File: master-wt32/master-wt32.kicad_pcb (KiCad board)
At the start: 2 copper layers, 52.3 x 72.4 mm, 4 parts, among them J1 Conn_01x06_Male, J2 Conn_01x06_Male, J3 Conn_01x06_Female, J4 Conn_01x06_Female

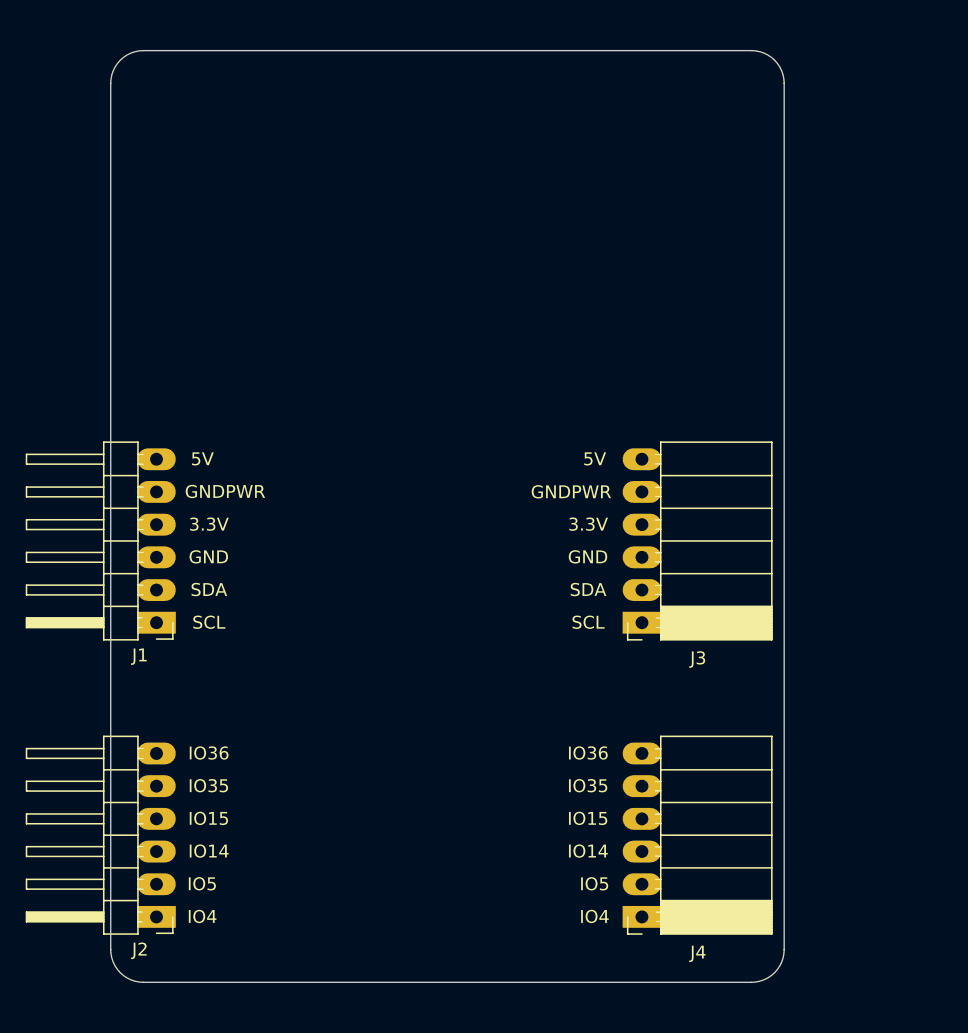
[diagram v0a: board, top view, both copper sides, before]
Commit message: add components to master-wt32
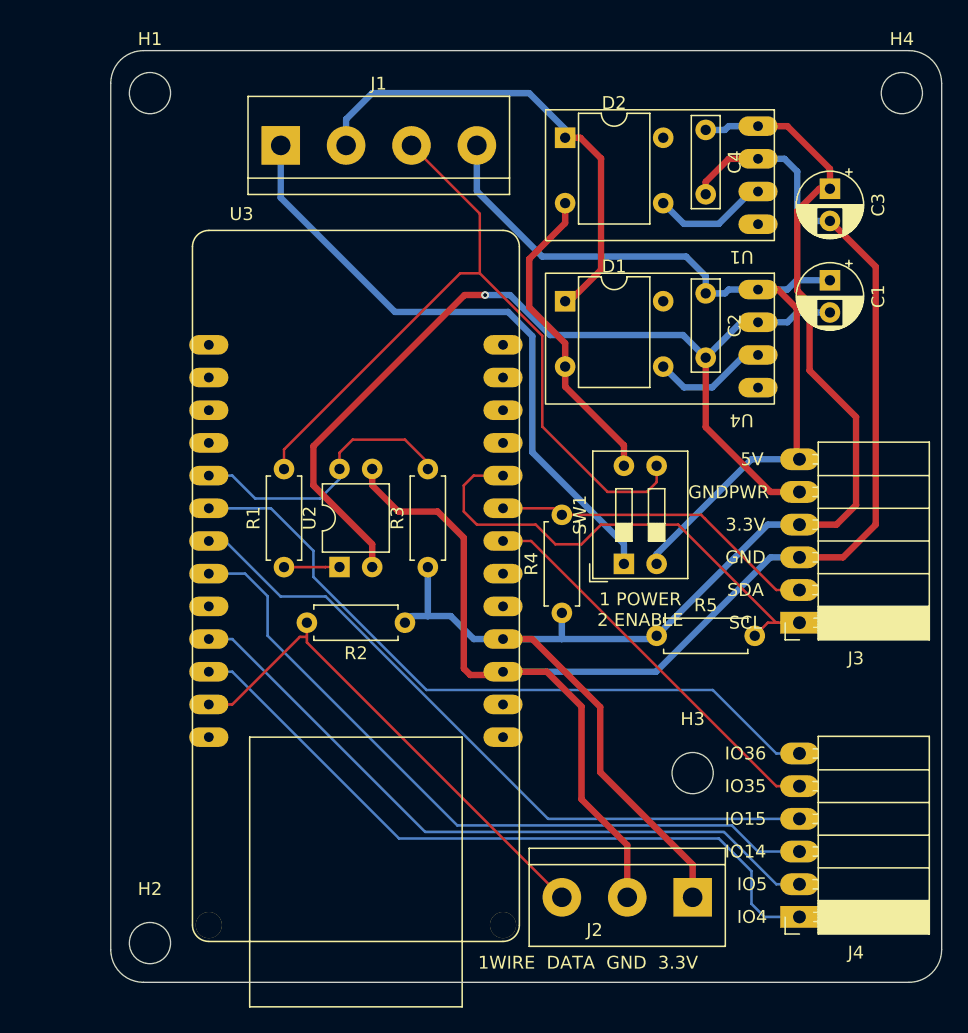
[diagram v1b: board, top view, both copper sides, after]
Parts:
- added C1: 1uF 50V, Capacitor_THT:CP_Radial_D5.0mm_P2.50mm, F.Cu at (119.4, 72.5)
- added C2: 100nF 63V, Capacitor_THT:C_Rect_L7.0mm_W2.0mm_P5.00mm, F.Cu at (109.7, 73.5)
- added C3: 1uF 50V, Capacitor_THT:CP_Radial_D5.0mm_P2.50mm, F.Cu at (119.4, 65.3)
- added C4: 100nF 63V, Capacitor_THT:C_Rect_L7.0mm_W2.0mm_P5.00mm, F.Cu at (109.7, 60.8)
- added D1: DB107, custom:DB107, F.Cu at (98.8, 74.1)
- added D2: DB107, custom:DB107, F.Cu at (98.8, 61.4)
- added H1: MountingHole, MountingHole:MountingHole_3.2mm_M3, F.Cu at (66.5, 57.9)
- added H2: MountingHole, MountingHole:MountingHole_3.2mm_M3, F.Cu at (66.5, 124.0)
- added H3: MountingHole, MountingHole:MountingHole_3.2mm_M3, F.Cu at (108.7, 110.7)
- added H4: MountingHole, MountingHole:MountingHole_3.2mm_M3, F.Cu at (125.0, 57.9)
- added R1: 680, Resistor_THT:R_Axial_DIN0207_L6.3mm_D2.5mm_P7.62mm_Horizontal, F.Cu at (77.0, 94.7)
- added R2: 4k7, Resistor_THT:R_Axial_DIN0207_L6.3mm_D2.5mm_P7.62mm_Horizontal, F.Cu at (86.4, 99.1)
- added R3: 10k, Resistor_THT:R_Axial_DIN0207_L6.3mm_D2.5mm_P7.62mm_Horizontal, F.Cu at (88.1, 94.7)
- added R4: 10k, Resistor_THT:R_Axial_DIN0207_L6.3mm_D2.5mm_P7.62mm_Horizontal, F.Cu at (98.6, 98.3)
- added R5: 10k, Resistor_THT:R_Axial_DIN0207_L6.3mm_D2.5mm_P7.62mm_Horizontal, F.Cu at (105.9, 100.1)
- added SW1: SW_DIP_x02, Button_Switch_THT:SW_DIP_SPSTx02_Slide_9.78x7.26mm_W7.62mm_P2.54mm, F.Cu at (103.4, 94.5)
- added U1: MINI360, boards:MINI360, F.Cu at (106.2, 64.3)
- added U2: PC817, Package_DIP:DIP-4_W7.62mm, F.Cu at (81.3, 94.7)
- added U3: WT32-ETH0-Board, boards:WT32-ETH01-Board-Reversed, F.Cu at (82.5, 96.5)
- added U4: MINI360, boards:MINI360, F.Cu at (106.2, 77.0)
- J1: value Conn_01x06_Male -> Screw_Terminal_01x04; footprint Connector_PinHeader_2.54mm:PinHeader_1x06_P2.54mm_Horizontal -> TerminalBlock:TerminalBlock_bornier-4_P5.08mm
- J2: value Conn_01x06_Male -> Screw_Terminal_01x03; footprint Connector_PinHeader_2.54mm:PinHeader_1x06_P2.54mm_Horizontal -> TerminalBlock:TerminalBlock_bornier-3_P5.08mm
- moved J2 41.7 mm to (108.7, 120.4)
- moved J1 38.3 mm to (76.7, 62.0), turned to 0 degrees
- moved J3 12.2 mm to (117.0, 99.1)
- moved J4 12.2 mm to (117.0, 121.9)
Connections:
- J1 pad 1: SCL -> Net-(J1-Pad1)
- J1 pad 2: SDA -> IN-
- J1 pad 3: GND -> ENABLE_IN
- J1 pad 4: +3V3 -> +5V
- J2 pad 1: GPIO4 -> +3V3
- J2 pad 2: GPIO5 -> GND
- J2 pad 3: GPIO14 -> 1WIRE
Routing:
- net GND: track 0.00 -> 121.0 mm
- net +3V3: track 0.00 -> 114.4 mm
- net GNDPWR: track 0.00 -> 74.5 mm, vias 0 -> 1
- net +5V: track 0.00 -> 65.8 mm
- net ENABLE_IN: track 0.00 -> 61.0 mm
- net GPIO14: track 0.00 -> 56.6 mm
- net GPIO4: track 0.00 -> 55.3 mm
- net GPIO36: track 0.00 -> 55.0 mm
- net GPIO15: track 0.00 -> 54.8 mm
- net GPIO5: track 0.00 -> 53.8 mm
- net Net-(J1-Pad1): track 0.00 -> 48.7 mm
- net 1WIRE: track 0.00 -> 39.3 mm
- net SCL: track 0.00 -> 38.5 mm
- net IN-: track 0.00 -> 37.6 mm
- net GPIO35: track 0.00 -> 30.9 mm
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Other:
- board size 52.3 x 72.4 mm -> 64.6 x 72.4 mm
- board text added: "1 POWER 2 ENABLE"
- board text added: "1WIRE DATA GND 3.3V"

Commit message: route master-wt32
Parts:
- added D3: LED, LED_THT:LED_D5.0mm, F.Cu at (105.9, 87.1)
- added D4: LED, LED_THT:LED_D5.0mm, F.Cu at (98.5, 87.1)
- added R6: 330, Resistor_THT:R_Axial_DIN0207_L6.3mm_D2.5mm_P7.62mm_Horizontal, F.Cu at (110.2, 94.0)
- added R7: 680, Resistor_THT:R_Axial_DIN0207_L6.3mm_D2.5mm_P7.62mm_Horizontal, F.Cu at (98.6, 94.0)
- moved R5 21.8 mm to (84.3, 102.9), turned to 90 degrees
- moved R1 13.5 mm to (76.7, 81.3)
- moved R2 13.5 mm to (86.1, 85.6)
- moved R3 13.5 mm to (87.9, 81.3)
- moved U2 13.5 mm to (81.0, 81.3)
- moved R4 11.4 mm to (88.1, 102.9)
- moved SW1 7.37 mm to (103.1, 101.9)
- moved C1 1.08 mm to (120.1, 73.2)
- moved C3 0.92 mm to (120.1, 65.9)
- moved C2 0.28 mm to (109.7, 73.2)
- moved C4 0.28 mm to (109.7, 60.5)
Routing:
- net +5V: track 65.8 -> 109.4 mm
- net Net-(J1-Pad1): track 48.7 -> 75.1 mm
- net GND: track 121.0 -> 139.7 mm
- net SCL: track 38.5 -> 56.8 mm
- net +3V3: track 114.4 -> 132.2 mm
- net 1WIRE: track 39.3 -> 53.1 mm
- net SDA: track 25.7 -> 36.7 mm
- net ENABLE: track 22.1 -> 31.5 mm
- net Net-(D3-Pad1): track 0.00 -> 8.65 mm
- net GPIO35: track 30.9 -> 39.3 mm
- net IN+: track 24.6 -> 31.9 mm
- net Net-(D4-Pad1): track 0.00 -> 6.86 mm
- net ENABLE_IN: track 61.0 -> 67.9 mm
- net GNDPWR: track 74.5 -> 67.8 mm, vias 1 -> 0
- net GPIO36: track 55.0 -> 60.2 mm
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
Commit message: refactor master-wt32 pcb
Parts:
- moved H2 86.7 mm to (123.9, 58.9)
- moved H4 65.5 mm to (123.9, 123.4)
- moved H3 43.5 mm to (67.1, 123.4)
- moved R6 36.5 mm to (83.6, 69.1), turned to 180 degrees
- moved R7 25.2 mm to (94.5, 69.1), turned to 180 degrees
- moved J4 5.07 mm to (116.5, 116.9)
- moved J3 2.62 mm to (116.5, 96.5)
- moved H1 1.14 mm to (67.1, 58.9)
- moved R4 0.92 mm to (88.9, 102.4)
- moved R5 0.92 mm to (85.1, 102.4)
- moved U4 0.92 mm to (106.9, 76.5)
- moved D2 0.92 mm to (99.6, 60.9)
- moved U1 0.92 mm to (106.9, 63.8)
- moved C2 0.92 mm to (110.5, 72.7)
- moved C3 0.92 mm to (120.9, 65.3)
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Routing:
- net GND: track 139.7 -> 0.00 mm
- net +3V3: track 132.2 -> 0.00 mm
- net +5V: track 109.4 -> 0.00 mm
- net Net-(J1-Pad1): track 75.1 -> 0.00 mm
- net ENABLE_IN: track 67.9 -> 0.00 mm
- net GNDPWR: track 67.8 -> 0.00 mm
- net GPIO36: track 60.2 -> 0.00 mm
- net GPIO15: track 58.1 -> 0.00 mm
- net GPIO14: track 57.7 -> 0.00 mm
- net SCL: track 56.8 -> 0.00 mm
- net GPIO4: track 54.8 -> 0.00 mm
- net GPIO5: track 53.8 -> 0.00 mm
- net 1WIRE: track 53.1 -> 0.00 mm
- net GPIO35: track 39.3 -> 0.00 mm
- net IN-: track 36.9 -> 0.00 mm
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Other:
- board size 64.6 x 72.4 mm -> 64 x 71.6 mm

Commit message: refactor master-wt32
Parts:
- removed C1: 1uF 50V, Capacitor_THT:CP_Radial_D5.0mm_P2.50mm
- removed C2: 100nF 63V, Capacitor_THT:C_Rect_L7.0mm_W2.0mm_P5.00mm
- removed D2: DB107, custom:DB107
- removed D3: LED, LED_THT:LED_D5.0mm
- removed R6: 330, Resistor_THT:R_Axial_DIN0207_L6.3mm_D2.5mm_P7.62mm_Horizontal
- removed SW1: SW_DIP_x02, Button_Switch_THT:SW_DIP_SPSTx02_Slide_9.78x7.26mm_W7.62mm_P2.54mm
- C3: value 1uF 50V -> 100nF 63V; footprint Capacitor_THT:CP_Radial_D5.0mm_P2.50mm -> Capacitor_THT:C_Rect_L7.0mm_W2.0mm_P5.00mm
- C4: value 100nF 63V -> 10uF 50V; footprint Capacitor_THT:C_Rect_L7.0mm_W2.0mm_P5.00mm -> Capacitor_THT:CP_Radial_D5.0mm_P2.50mm
- U1: value MINI360 -> LM2596-Board; footprint boards:MINI360 -> boards:LM2596-Board
- U4: value MINI360 -> LD1117S33TR_SOT223; footprint boards:MINI360 -> Package_TO_SOT_THT:TO-220-3_Vertical
- moved C4 48.8 mm to (101.6, 108.0), turned to 180 degrees
- moved D4 22.7 mm to (120.7, 78.7)
- moved C3 20.7 mm to (104.1, 77.5)
- moved U4 17.7 mm to (124.1, 72.4), turned to 90 degrees
- moved R7 16.3 mm to (108.5, 77.5), turned to 0 degrees
- moved U1 16.3 mm to (108.0, 80.0), turned to -90 degrees
- moved D1 4.86 mm to (104.3, 72.4), turned to 90 degrees
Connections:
- C3 pad 1: +3V3 -> +5V
- C3 pad 2: GND -> GNDPWR
- C4 pad 2: GND -> GNDPWR
- J1 pad 1: Net-(J1-Pad1) -> IN+
- J2 pad 2: GND -> GNDPWR
- J3 pad 3: GND -> GNDPWR
- U1 pad 1: unconnected-(U1-Pad1) -> Net-(D1-Pad3)
- U1 pad 2: Net-(D2-Pad3) -> Net-(D1-Pad4)
- U1 pad 3: GND -> GNDPWR
- U1 pad 4: +3V3 -> +5V
- U2 pad 3: GND -> GNDPWR
- U3 pad 10: +3V3 -> unconnected-(U3-Pad10)
- U3 pad 11: GND -> GNDPWR
- U3 pad 12: unconnected-(U3-Pad12) -> +5V
- U4 pad 1: unconnected-(U4-Pad1) -> GNDPWR
- U4 pad 2: Net-(D1-Pad3) -> +3V3
- U4 pad 3: GNDPWR -> +5V
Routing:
- net +3V3: track 0.00 -> 141.1 mm
- net GNDPWR: track 0.00 -> 120.7 mm
- net +5V: track 0.00 -> 115.0 mm
- net 1WIRE: track 0.00 -> 65.9 mm
- net GPIO36: track 0.00 -> 59.4 mm
- net GPIO15: track 0.00 -> 56.1 mm
- net GPIO14: track 0.00 -> 53.0 mm
- net GPIO5: track 0.00 -> 50.9 mm
- net GPIO4: track 0.00 -> 50.9 mm
- net IN+: track 0.00 -> 45.5 mm
- net SCL: track 0.00 -> 42.5 mm
- net GPIO35: track 0.00 -> 41.1 mm
- net IN-: track 0.00 -> 33.6 mm
- net SDA: track 0.00 -> 32.2 mm
- net ENABLE: track 0.00 -> 28.1 mm
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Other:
- board text removed: "1 POWER 2 ENABLE"

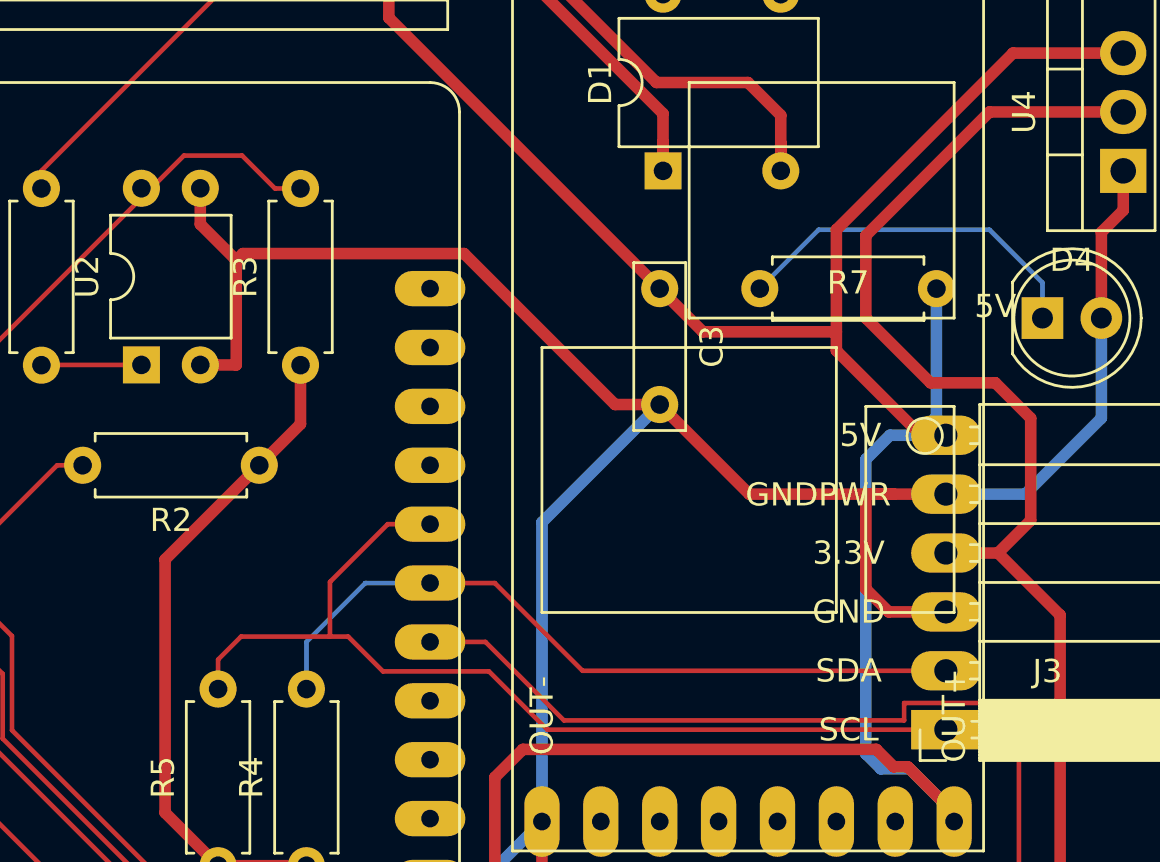
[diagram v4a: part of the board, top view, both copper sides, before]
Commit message: update master-wt32 routing
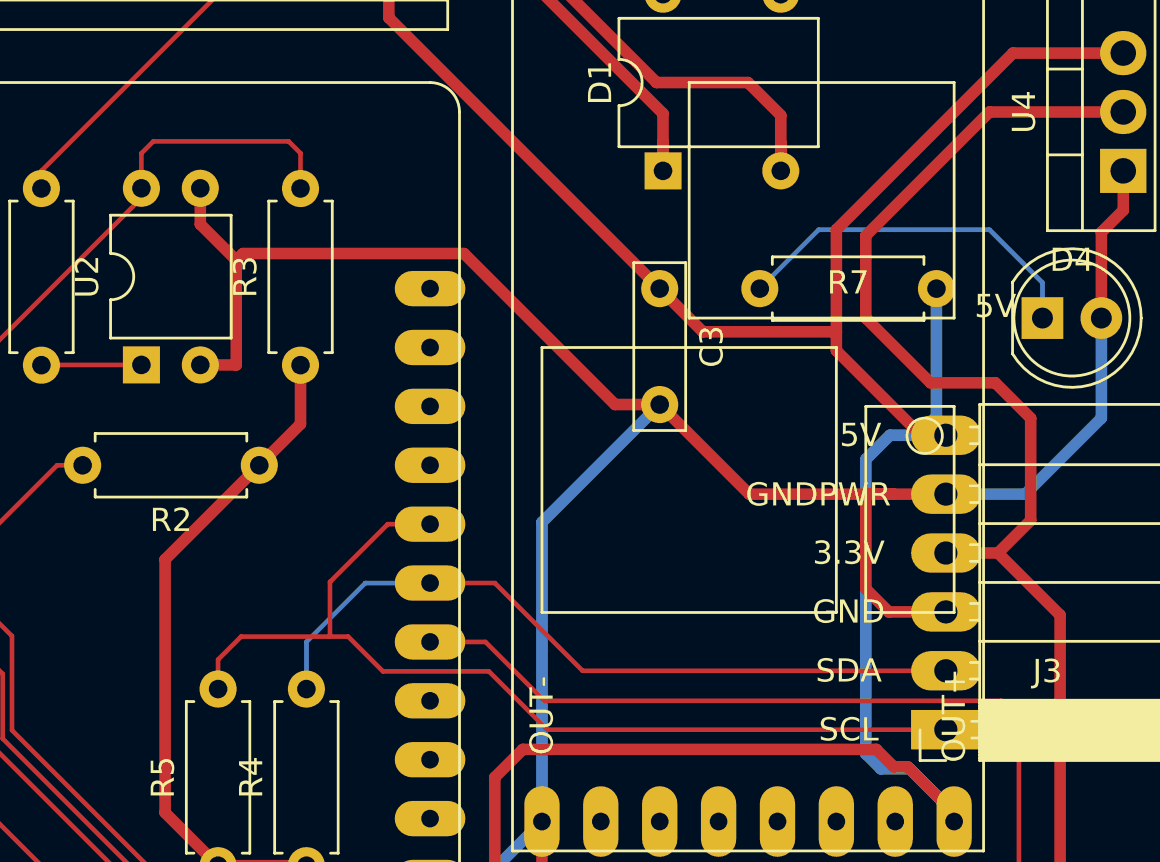
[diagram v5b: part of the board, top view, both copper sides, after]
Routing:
- net ENABLE: track 28.1 -> 30.8 mm
- net GPIO35: track 41.1 -> 40.0 mm
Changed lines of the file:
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@@
-(kicad_pcb (version 20210722) (generator pcbnew)
+(kicad_pcb (version 20210925) (generator pcbnew)
   (general
     (thickness 1.6)
@@
     (fp_circle (center 0 0) (end 3.2 0) (layer "Cmts.User") (width 0.15) (fill none))
     (fp_circle (center 0 0) (end 3.45 0) (layer "F.CrtYd") (width 0.05) (fill none))
-    (pad "1" np_thru_hole circle locked (at 0 0) (size 3.2 3.2) (drill 3.2) (layers *.Cu *.Mask))
+    (pad "" np_thru_hole circle locked (at 0 0) (size 3.2 3.2) (drill 3.2) (layers *.Cu *.Mask))
   )
   (footprint "boards:WT32-ETH01-Board-Reversed" (layer "F.Cu")
@@
     (fp_circle (center 0 0) (end 3.2 0) (layer "Cmts.User") (width 0.15) (fill none))
     (fp_circle (center 0 0) (end 3.45 0) (layer "F.CrtYd") (width 0.05) (fill none))
-    (pad "1" np_thru_hole circle locked (at 0 0) (size 3.2 3.2) (drill 3.2) (layers *.Cu *.Mask))
+    (pad "" np_thru_hole circle locked (at 0 0) (size 3.2 3.2) (drill 3.2) (layers *.Cu *.Mask))
   )
   (footprint "Package_DIP:DIP-4_W7.62mm" (layer "F.Cu")
@@
     (fp_circle (center 0 0) (end 3.2 0) (layer "Cmts.User") (width 0.15) (fill none))
     (fp_circle (center 0 0) (end 3.45 0) (layer "F.CrtYd") (width 0.05) (fill none))
-    (pad "1" np_thru_hole circle locked (at 0 0) (size 3.2 3.2) (drill 3.2) (layers *.Cu *.Mask))
+    (pad "" np_thru_hole circle locked (at 0 0) (size 3.2 3.2) (drill 3.2) (layers *.Cu *.Mask))
   )
   (footprint "LED_THT:LED_D5.0mm" (layer "F.Cu")
@@
     (fp_circle (center 0 0) (end 3.2 0) (layer "Cmts.User") (width 0.15) (fill none))
     (fp_circle (center 0 0) (end 3.45 0) (layer "F.CrtYd") (width 0.05) (fill none))
-    (pad "1" np_thru_hole circle locked (at 0 0) (size 3.2 3.2) (drill 3.2) (layers *.Cu *.Mask))
+    (pad "" np_thru_hole circle locked (at 0 0) (size 3.2 3.2) (drill 3.2) (layers *.Cu *.Mask))
   )
   (footprint "Capacitor_THT:C_Rect_L7.0mm_W2.0mm_P5.00mm" (layer "F.Cu")
@@
   (segment (start 105.918 111.506) (end 91.186 111.506) (width 0.2) (layer "F.Cu") (net 10))
   (segment (start 116.483 104.175) (end 113.249 104.175) (width 0.2) (layer "F.Cu") (net 10))
+  (segment (start 119.634 96.012) (end 118.872 95.25) (width 0.2) (layer "F.Cu") (net 11))
+  (segment (start 119.634 105.664) (end 119.634 96.012) (width 0.2) (layer "F.Cu") (net 11))
+  (segment (start 99.1644 95.25) (end 96.6244 92.71) (width 0.2) (layer "F.Cu") (net 11))
+  (segment (start 96.6244 92.71) (end 94.234 92.71) (width 0.2) (layer "F.Cu") (net 11))
+  (segment (start 118.872 95.25) (end 99.1644 95.25) (width 0.2) (layer "F.Cu") (net 11))
+  (segment (start 116.483 106.715) (end 116.4832 106.715) (width 0.2) (layer "F.Cu") (net 11))
+  (segment (start 118.583 106.715) (end 119.634 105.664) (width 0.2) (layer "F.Cu") (net 11))
   (segment (start 116.4832 106.715) (end 118.583 106.715) (width 0.2) (layer "F.Cu") (net 11))
-  (segment (start 114.684 95.3455) (end 114.684 96.0955) (width 0.2) (layer "F.Cu") (net 11))
-  (segment (start 96.6244 92.71) (end 94.234 92.71) (width 0.2) (layer "F.Cu") (net 11))
-  (segment (start 118.583 106.715) (end 119.634 105.664) (width 0.2) (layer "F.Cu") (net 11))
-  (segment (start 100.01 96.0955) (end 96.6244 92.71) (width 0.2) (layer "F.Cu") (net 11))
-  (segment (start 116.483 106.715) (end 116.4832 106.715) (width 0.2) (layer "F.Cu") (net 11))
-  (segment (start 118.967 95.3455) (end 114.684 95.3455) (width 0.2) (layer "F.Cu") (net 11))
-  (segment (start 119.634 105.664) (end 119.634 96.012) (width 0.2) (layer "F.Cu") (net 11))
-  (segment (start 119.634 96.012) (end 118.967 95.3455) (width 0.2) (layer "F.Cu") (net 11))
-  (segment (start 114.684 96.0955) (end 100.01 96.0955) (width 0.2) (layer "F.Cu") (net 11))
   (segment (start 116.483 111.795) (end 111.979 111.795) (width 0.2) (layer "F.Cu") (net 12))
   (segment (start 116.483 111.795) (end 116.4832 111.795) (width 0.2) (layer "F.Cu") (net 12))
@@
   (segment (start 81.783 80.762) (end 77.48 80.762) (width 0.2) (layer "F.Cu") (net 19))
   (segment (start 77.48 80.762) (end 77.47 80.772) (width 0.2) (layer "F.Cu") (net 19))
+  (segment (start 81.783 71.633) (end 82.296 71.12) (width 0.2) (layer "F.Cu") (net 20))
+  (segment (start 88.646 71.628) (end 88.646 73.152) (width 0.2) (layer "F.Cu") (net 20))
   (segment (start 71.374 87.63) (end 73.1983 87.63) (width 0.2) (layer "F.Cu") (net 20))
-  (segment (start 86.1238 71.7301) (end 83.6163 71.7301) (width 0.2) (layer "F.Cu") (net 20))
+  (segment (start 81.783 73.142) (end 81.783 71.633) (width 0.2) (layer "F.Cu") (net 20))
   (segment (start 73.1983 87.63) (end 73.1983 82.1481) (width 0.2) (layer "F.Cu") (net 20))
-  (segment (start 87.5457 73.152) (end 86.1238 71.7301) (width 0.2) (layer "F.Cu") (net 20))
   (segment (start 81.783 73.142) (end 82.2044 73.142) (width 0.2) (layer "F.Cu") (net 20))
-  (segment (start 88.646 73.152) (end 87.5457 73.152) (width 0.2) (layer "F.Cu") (net 20))
-  (segment (start 83.6163 71.7301) (end 82.2044 73.142) (width 0.2) (layer "F.Cu") (net 20))
+  (segment (start 82.296 71.12) (end 88.138 71.12) (width 0.2) (layer "F.Cu") (net 20))
+  (segment (start 88.138 71.12) (end 88.646 71.628) (width 0.2) (layer "F.Cu") (net 20))
   (segment (start 73.1983 82.1481) (end 82.2044 73.142) (width 0.2) (layer "F.Cu") (net 20))
   (segment (start 110.998 74.93) (end 118.364 74.93) (width 0.2) (layer "B.Cu") (net 34))

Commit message: add master-wt32-1.0 label
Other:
- board text added: "master-wt32-1.0"
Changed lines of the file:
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@@
     (effects (font (size 1 1) (thickness 0.15)))
+  )
+  (gr_text "master-wt32-1.0" (at 66.294 93.218 90) (layer "F.SilkS")
+    (effects (font (size 1.5 1.5) (thickness 0.3)))
   )
   (gr_text "5V" (at 112.8002 83.795) (layer "F.SilkS")
